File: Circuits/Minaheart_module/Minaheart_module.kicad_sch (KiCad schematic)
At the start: 1 part, among them U1 ESP32-C3-DevKitM-1

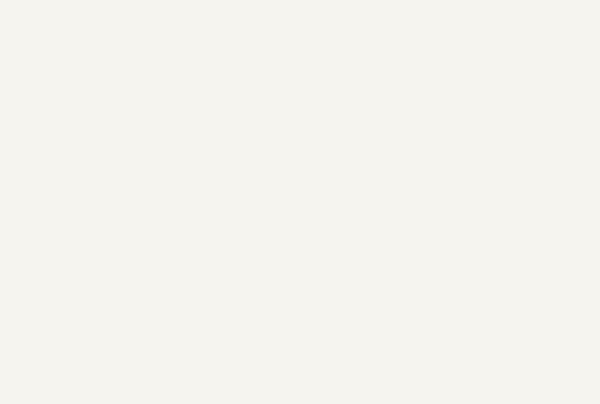
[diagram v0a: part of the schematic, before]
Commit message: Add the circuit, add the Minami model rocket project
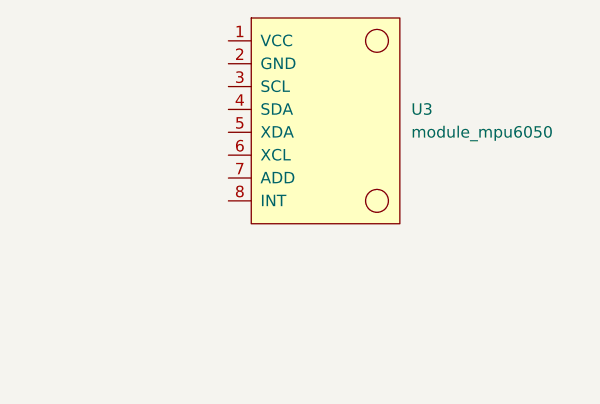
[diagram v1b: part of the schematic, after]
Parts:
- added U3: module_mpu6050, usini_sensors:module_mpu6050, symbol usini_sensors:module_mpu6050
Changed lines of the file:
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@@
+	)
+	(symbol
+		(lib_id "usini_sensors:module_mpu6050")
+		(at 184.15 55.88 0)
+		(unit 1)
+		(exclude_from_sim no)
+		(in_bom yes)
+		(on_board yes)
+		(dnp no)
+		(fields_autoplaced yes)
+		(property "Reference" "U3"
+			(at 204.47 45.7199 0)
+			(effects
+				(font
+					(size 1.27 1.27)
+				)
+				(justify left)
+			)
+		)
+		(property "Value" "module_mpu6050"
+			(at 204.47 48.2599 0)
+			(effects
+				(font
+					(size 1.27 1.27)
+				)
+				(justify left)
+			)
+		)
+		(property "Footprint" "usini_sensors:module_mpu6050"
+			(at 195.58 62.23 0)
+			(effects
+				(font
+					(size 1.27 1.27)
+				)
+				(hide yes)
+			)
+		)
+		(property "Datasheet" ""
+			(at 184.15 49.53 0)
+			(effects
+				(font
+					(size 1.27 1.27)
+				)
+				(hide yes)
+			)
+		)
+		(property "Description" ""
+			(at 184.15 55.88 0)
+			(effects
+				(font
+					(size 1.27 1.27)
+				)
+				(hide yes)
+			)
+		)
+		(pin "6"
+		)
+		(pin "8"
+		)
+		(pin "1"
+		)
+		(pin "5"
+		)
+		(pin "3"
+		)
+		(pin "7"
+		)
+		(pin "4"
+		)
+		(pin "2"
+		)
+		(instances
+			(project ""
+				(path "/b169e324-7e63-4f2a-8267-145507483ee6"
+					(reference "U3")
+					(unit 1)
+				)
+			)
+		)
 	)
 	(symbol

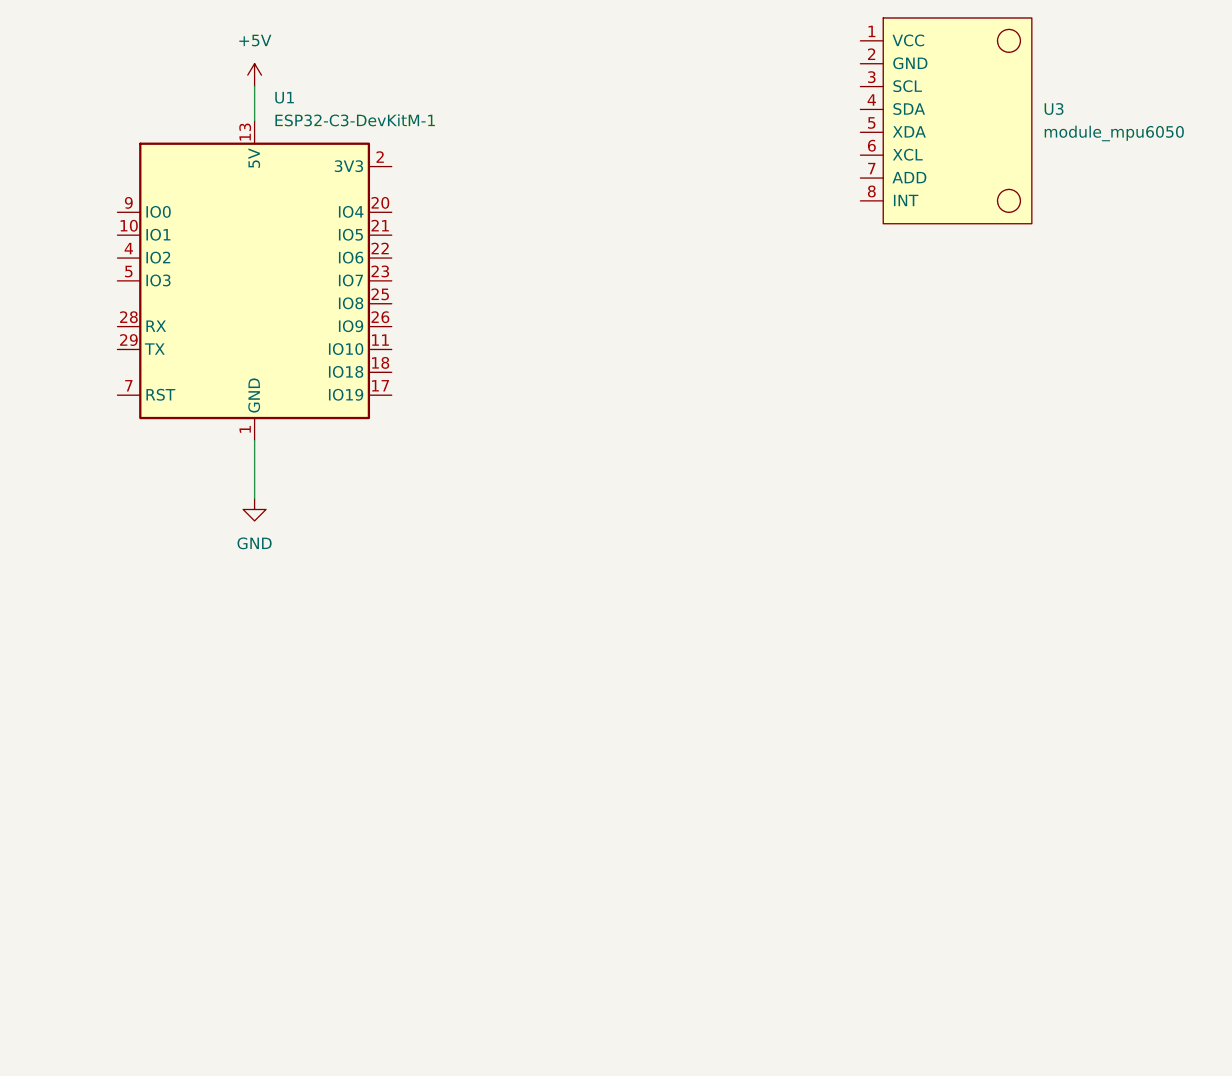
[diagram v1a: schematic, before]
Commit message: Replace the ESP32 with STM32
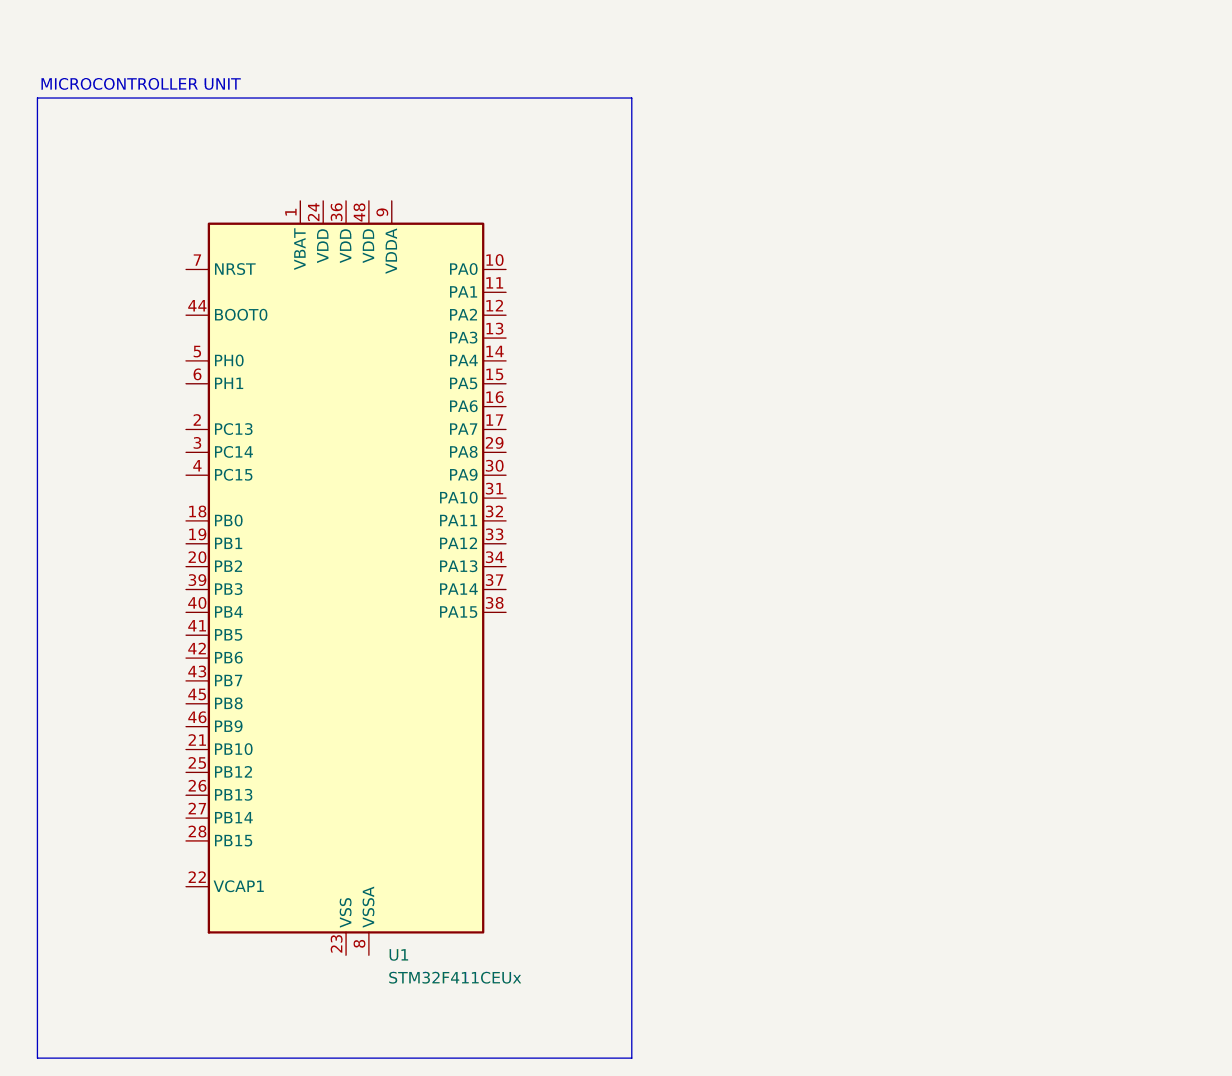
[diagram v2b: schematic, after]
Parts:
- removed U1: ESP32-C3-DevKitM-1, RF_Module:ESP32-C3-DevKitM-1, symbol RF_Module:ESP32-C3-DevKitM-1
- removed U3: module_mpu6050, usini_sensors:module_mpu6050, symbol usini_sensors:module_mpu6050
- added U1: STM32F411CEUx, Package_DFN_QFN:QFN-48-1EP_7x7mm_P0.5mm_EP5.6x5.6mm, symbol MCU_ST_STM32F4:STM32F411CEUx
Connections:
- new net: U1.23 (VSS), U1.35 (VSS), U1.47 (VSS), U1.49 (VSS)
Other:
- note added: "MICROCONTROLLER UNIT"
